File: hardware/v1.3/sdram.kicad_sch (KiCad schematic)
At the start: 8 parts, among them U1 ECP5-CABGA256, U10 W9825G6KH

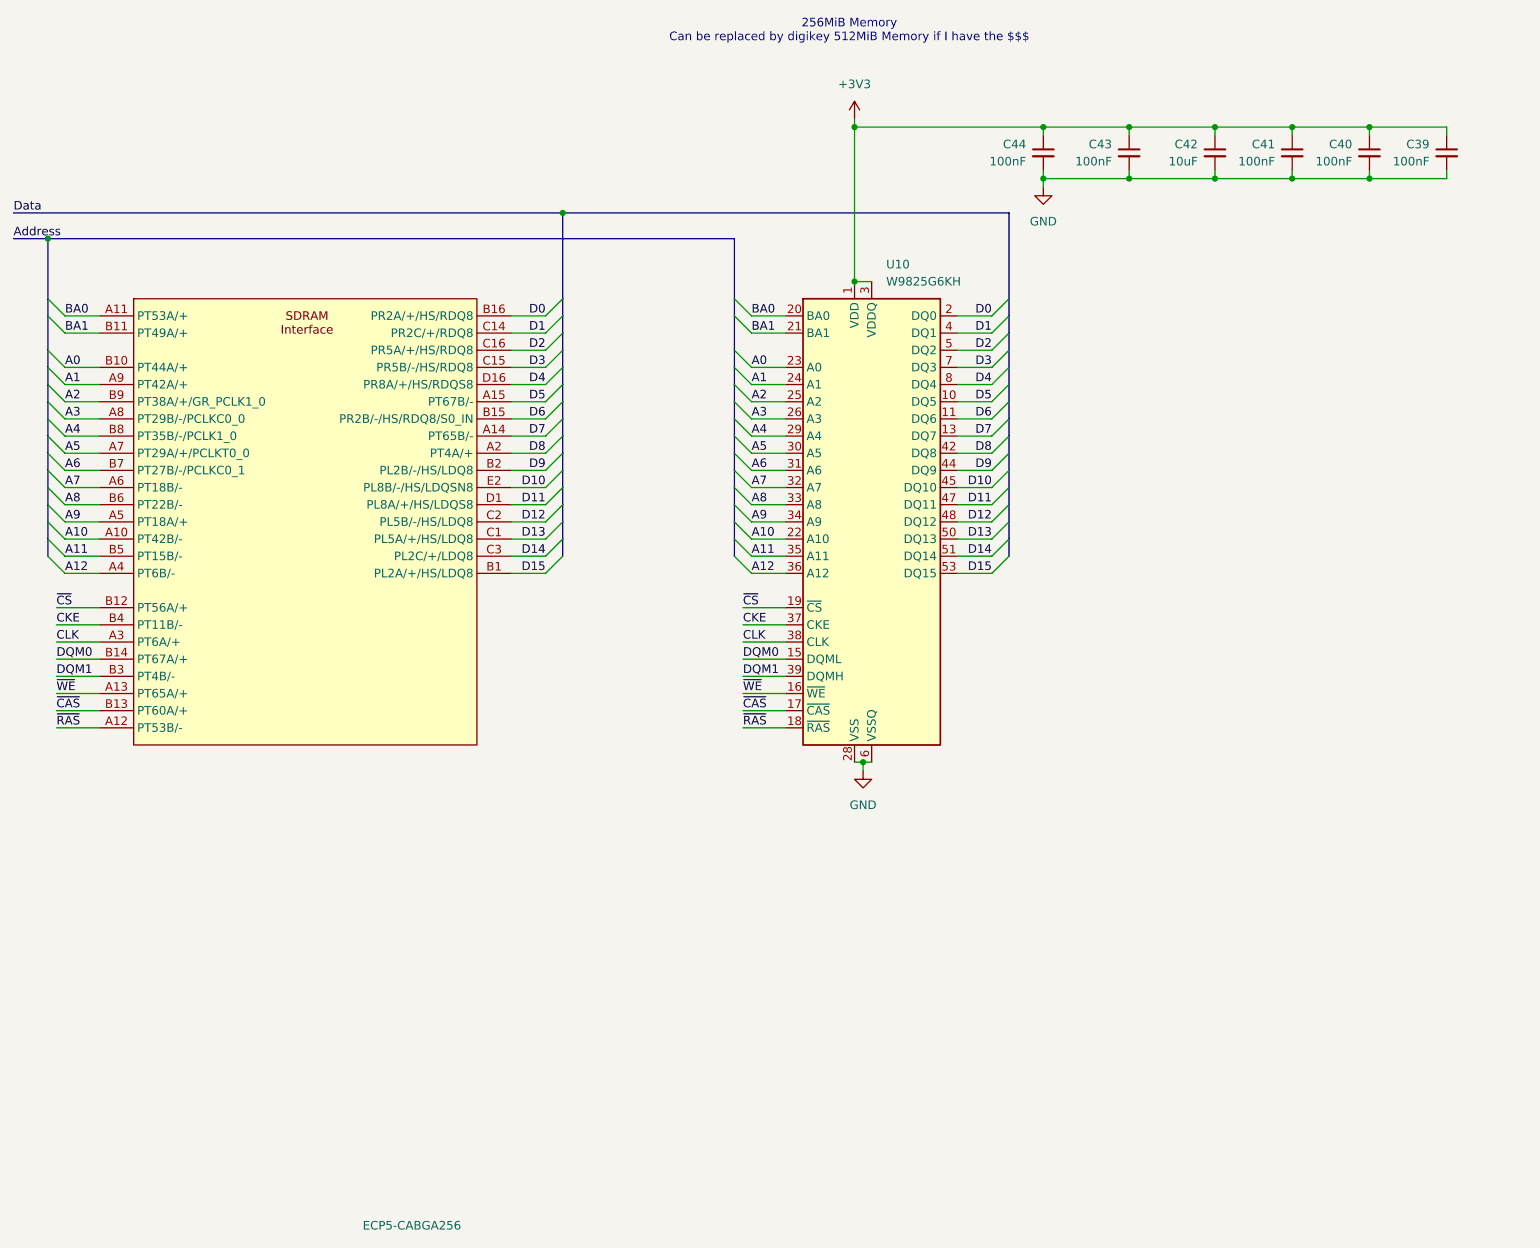
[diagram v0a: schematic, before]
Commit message: Refine README
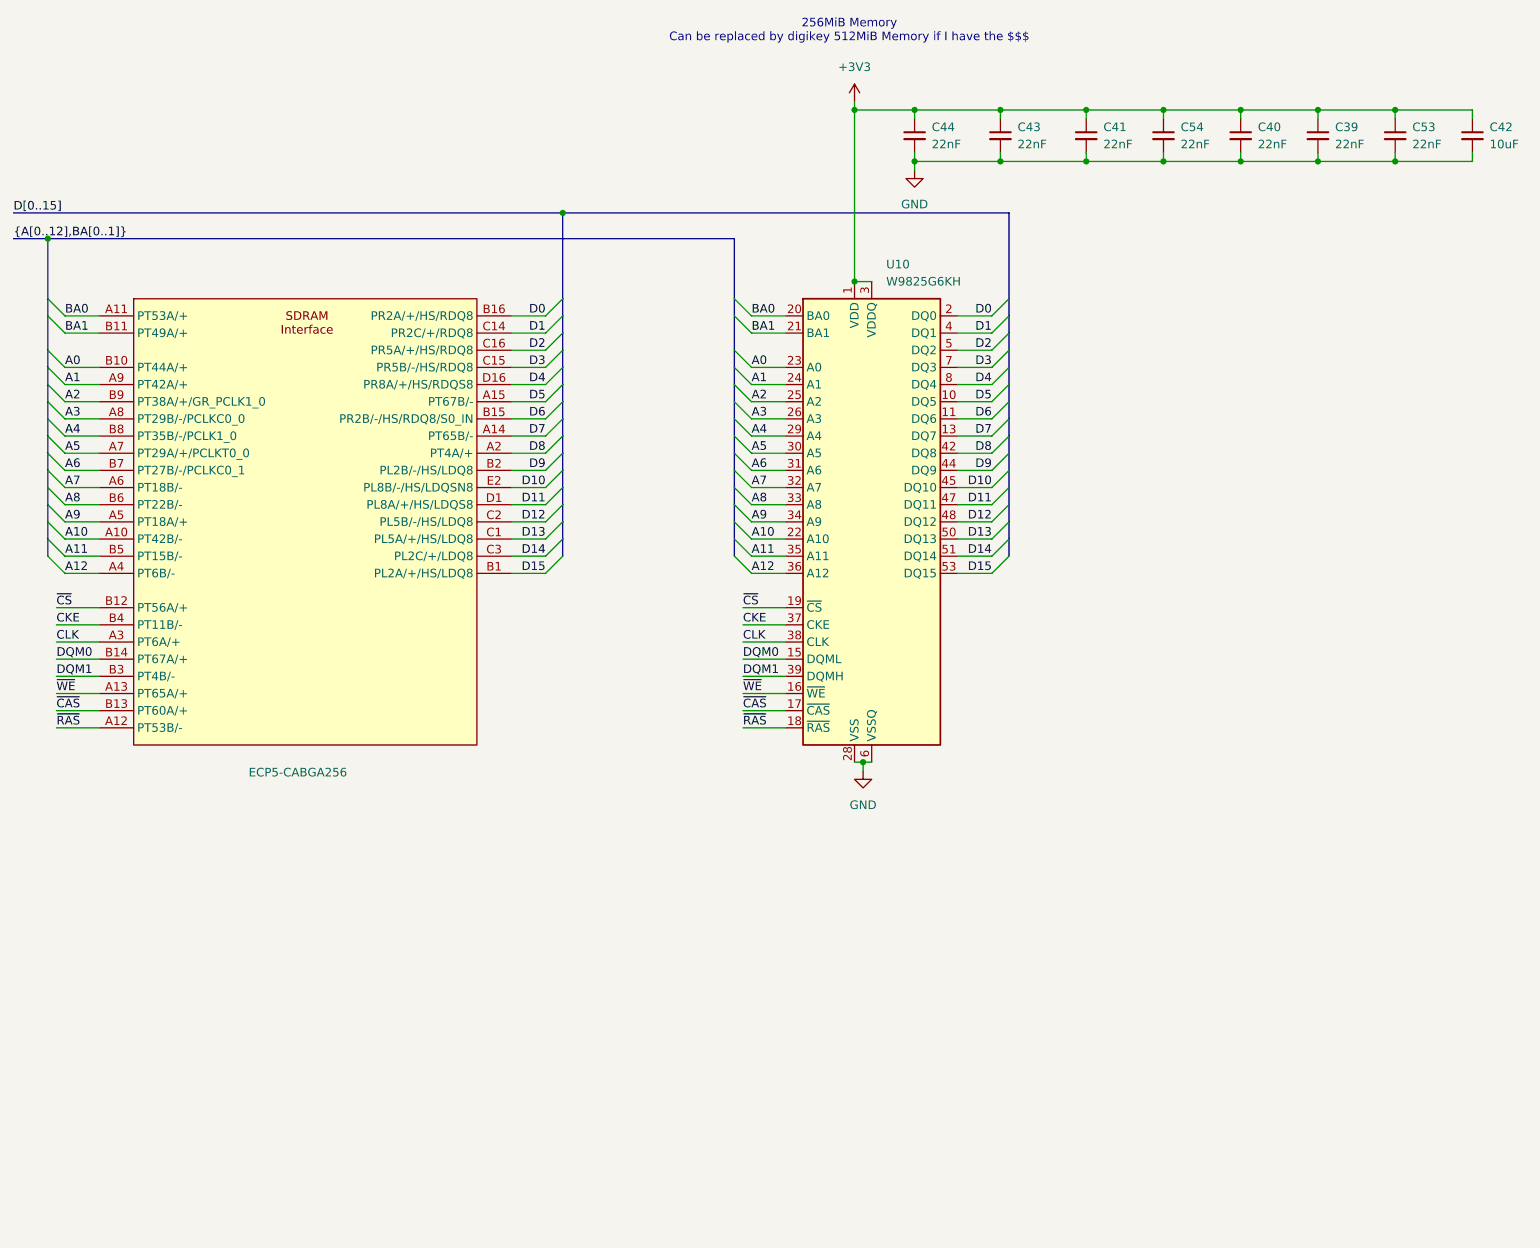
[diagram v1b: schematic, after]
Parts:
- added C53, C54: 22nF, Capacitor_SMD:C_0603_1608Metric, symbol Device:C_Small
- C39, C40, C41, C43, C44: value 100nF -> 22nF; footprint Capacitor_SMD:C_0402_1005Metric -> Capacitor_SMD:C_0603_1608Metric; LCSC Link (none) -> https://lcsc.com/product-detail/Multilayer-Ceramic-Capacito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; LCSC Part # C307331 -> C77571; Manufactuer Part Number (none) -> 0603B223K500NT
- C42: LCSC Link (none) -> https://lcsc.com/product-detail/Multilayer-Ceramic-Capacito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; Manufactuer Part Number (none) -> CL10A106KP8NNNC
- U1: LCSC Link (none) -> https://lcsc.com/product-detail/Programmable-Logic-Device-C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; LCSC Part # (none) -> C1521614; Manufactuer Part Number (none) -> LFE5U-25F-6BG256C
- U10: LCSC Link (none) -> https://lcsc.com/product-detail/SDRAM_Winbond-W9825G6KH-6_C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; Manufactuer Part Number (none) -> W9825G6KH-6
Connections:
- net +3V3: now also C53.1, C54.1
- net GND: now also C53.2, C54.2
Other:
- moved on the sheet: C39, C40, C41, C42, C43, C44

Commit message: Update files
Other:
- note added: "256MiB Memory Can be replaced by digikey 512MiB Memory there is the $$$"
- note removed: "256MiB Memory Can be replaced by digikey 512MiB Memory if I have the $$$"
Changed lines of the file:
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@@
 	(title_block
 		(title "Icepi zero")
-		(date "2025-06-16")
-		(rev "v1.2")
+		(date "2025-08-31")
+		(rev "v1.3")
 		(company "Chengyin Yao (cheyao)")
 		(comment 1 "https://github.com/cheyao/icepi-zero")
+		(comment 2 "License: Solderpad")
 		(comment 9 "OSHWA FR000026")
 	)
@@
 		(members)
 	)
-	(text "256MiB Memory\nCan be replaced by digikey 512MiB Memory if I have the $$$"
+	(text "256MiB Memory\nCan be replaced by digikey 512MiB Memory there is the $$$"
 		(exclude_from_sim no)
 		(at 171.958 27.686 0)

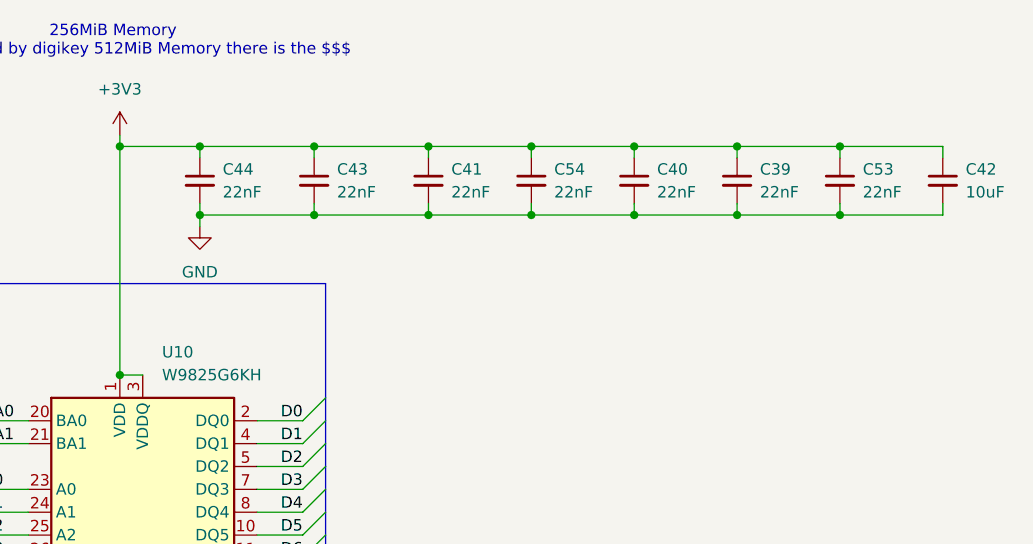
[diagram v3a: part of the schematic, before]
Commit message: Improve makefile and hardware
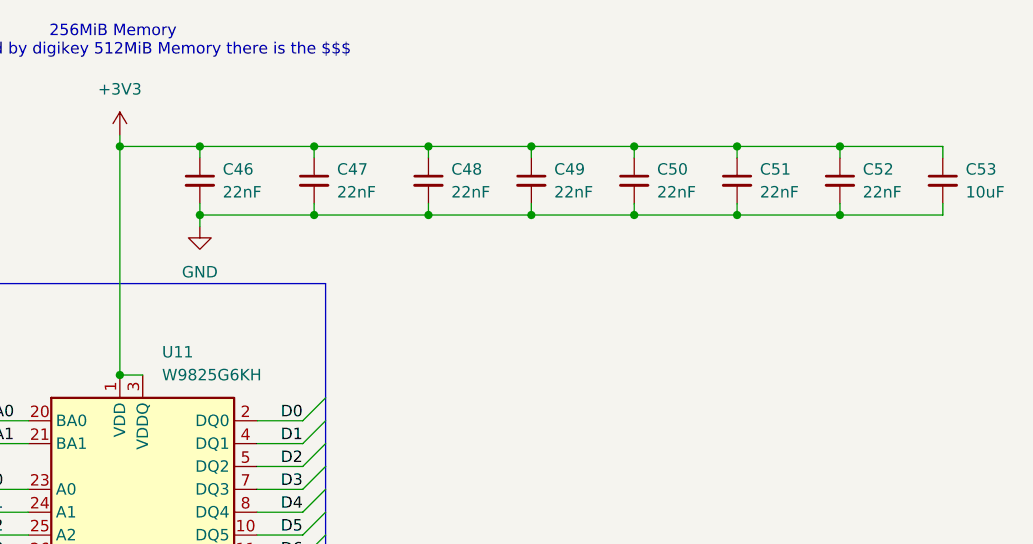
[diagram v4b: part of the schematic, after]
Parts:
- renumbered C44 to C46, C43 to C47, C41 to C48, C54 to C49, C40 to C50, C39 to C51, C53 to C52, C42 to C53, U10 to U11
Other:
- title: Icepi zero -> Icepi Zero
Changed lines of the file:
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@@
 	(paper "A4")
 	(title_block
-		(title "Icepi zero")
-		(date "2025-08-31")
+		(title "Icepi Zero")
+		(date "2025-10-10")
 		(rev "v1.3")
 		(company "Chengyin Yao (cheyao)")
@@
 		(dnp no)
 		(fields_autoplaced yes)
-		(property "Reference" "#PWR071"
+		(property "Reference" "#PWR081"
 			(at 172.72 41.91 0)
 			(effects
@@
 			(project "icepi-zero"
 				(path "/f88da08e-cf42-4d03-a08f-3f602fe6658d/3bffbb9a-e009-498c-a1b0-c490cdf30139"
-					(reference "#PWR071")
+					(reference "#PWR081")
 					(unit 1)
 				)
@@
 		(dnp no)
 		(fields_autoplaced yes)
-		(property "Reference" "C54"
+		(property "Reference" "C49"
 			(at 220.98 41.9162 0)
 			(effects
@@
 			(project "icepi-zero"
 				(path "/f88da08e-cf42-4d03-a08f-3f602fe6658d/3bffbb9a-e009-498c-a1b0-c490cdf30139"
-					(reference "C54")
+					(reference "C49")
 					(unit 1)
 				)
@@
 		(dnp no)
 		(fields_autoplaced yes)
-		(property "Reference" "C43"
+		(property "Reference" "C47"
 			(at 196.85 41.9162 0)
 			(effects
@@
 			(project "icepi-zero"
 				(path "/f88da08e-cf42-4d03-a08f-3f602fe6658d/3bffbb9a-e009-498c-a1b0-c490cdf30139"
-					(reference "C43")
+					(reference "C47")
 					(unit 1)
 				)
@@
 		(dnp no)
 		(fields_autoplaced yes)
-		(property "Reference" "C41"
+		(property "Reference" "C48"
 			(at 209.55 41.9162 0)
 			(effects
@@
 			(project "icepi-zero"
 				(path "/f88da08e-cf42-4d03-a08f-3f602fe6658d/3bffbb9a-e009-498c-a1b0-c490cdf30139"
-					(reference "C41")
+					(reference "C48")
 					(unit 1)
 				)
@@
 		(dnp no)
 		(fields_autoplaced yes)
-		(property "Reference" "C44"
+		(property "Reference" "C46"
 			(at 184.15 41.9162 0)
 			(effects
@@
 			(project "icepi-zero"
 				(path "/f88da08e-cf42-4d03-a08f-3f602fe6658d/3bffbb9a-e009-498c-a1b0-c490cdf30139"
-					(reference "C44")
+					(reference "C46")
 					(unit 1)
 				)
@@
 		(dnp no)
 		(fields_autoplaced yes)
-		(property "Reference" "U10"
+		(property "Reference" "U11"
 			(at 177.4033 62.23 0)
 			(effects
@@
 			(project "icepi-zero"
 				(path "/f88da08e-cf42-4d03-a08f-3f602fe6658d/3bffbb9a-e009-498c-a1b0-c490cdf30139"
-					(reference "U10")
+					(reference "U11")
 					(unit 1)
 				)
@@
 		(dnp no)
 		(fields_autoplaced yes)
-		(property "Reference" "#PWR073"
+		(property "Reference" "#PWR083"
 			(at 173.99 143.51 0)
 			(effects
@@
 			(project "icepi-zero"
 				(path "/f88da08e-cf42-4d03-a08f-3f602fe6658d/3bffbb9a-e009-498c-a1b0-c490cdf30139"
-					(reference "#PWR073")
+					(reference "#PWR083")
 					(unit 1)
 				)
@@
 		(dnp no)
 		(fields_autoplaced yes)
-		(property "Reference" "C40"
+		(property "Reference" "C50"
 			(at 232.41 41.9162 0)
 			(effects
@@
 			(project "icepi-zero"
 				(path "/f88da08e-cf42-4d03-a08f-3f602fe6658d/3bffbb9a-e009-498c-a1b0-c490cdf30139"
-					(reference "C40")
+					(reference "C50")
 					(unit 1)
 				)
@@
 		(dnp no)
 		(fields_autoplaced yes)
-		(property "Reference" "C39"
+		(property "Reference" "C51"
 			(at 243.84 41.9162 0)
 			(effects
@@
 			(project "icepi-zero"
 				(path "/f88da08e-cf42-4d03-a08f-3f602fe6658d/3bffbb9a-e009-498c-a1b0-c490cdf30139"
-					(reference "C39")
+					(reference "C51")
 					(unit 1)
 				)
@@
 		(dnp no)
 		(fields_autoplaced yes)
-		(property "Reference" "C53"
+		(property "Reference" "C52"
 			(at 255.27 41.9162 0)
 			(effects
@@
 			(project "icepi-zero"
 				(path "/f88da08e-cf42-4d03-a08f-3f602fe6658d/3bffbb9a-e009-498c-a1b0-c490cdf30139"
-					(reference "C53")
+					(reference "C52")
 					(unit 1)
 				)
@@
 		(dnp no)
 		(fields_autoplaced yes)
-		(property "Reference" "#PWR072"
+		(property "Reference" "#PWR082"
 			(at 181.61 54.61 0)
 			(effects
@@
 			(project "icepi-zero"
 				(path "/f88da08e-cf42-4d03-a08f-3f602fe6658d/3bffbb9a-e009-498c-a1b0-c490cdf30139"
-					(reference "#PWR072")
+					(reference "#PWR082")
 					(unit 1)
 				)
@@
 		(on_board yes)
 		(dnp no)
-		(property "Reference" "C42"
+		(property "Reference" "C53"
 			(at 266.7 41.9162 0)
 			(effects
@@
 			(project "icepi-zero"
 				(path "/f88da08e-cf42-4d03-a08f-3f602fe6658d/3bffbb9a-e009-498c-a1b0-c490cdf30139"
-					(reference "C42")
+					(reference "C53")
 					(unit 1)
 				)
